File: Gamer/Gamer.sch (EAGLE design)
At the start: 44 parts, among them J1 HEADER-1X8, J2 HEADER-1X8, J3 HEADER-1X8, J4 HEADER-1X8, J5 HEADER-1X8, J6 HEADER-1X8, J7 HEADER-1X8, J8 HEADER-1X8, U1 MMA8653FCR1, U2 ATTINY48, U3 ULN2803AFWG, U4 ATTINY48, U5 ULN2803AFWG, U6 ATTINY48, U7 ULN2803AFWG, U8 ATTINY48, U9 ULN2803AFWG

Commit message: gamer - ERC passes (with many okay warnings)
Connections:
- net 3V3 renamed VCC
- removed net N$1: START.4
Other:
- note added: "3.3V"
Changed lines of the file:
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@@
 <text x="96.52" y="96.52" size="3.81" layer="91">RasPi Header</text>
 <text x="187.96" y="76.2" size="3.81" layer="91">Accelerometer</text>
+<text x="97.79" y="159.766" size="1.778" layer="91" rot="R90">3.3V</text>
 </plain>
 <instances>
@@
 </segment>
 </net>
-<net name="3V3" class="0">
+<net name="VCC" class="0">
 <segment>
 <pinref part="SUPPLY17" gate="G$1" pin="VCC"/>
@@
 </segment>
 <segment>
-<label x="96.52" y="157.48" size="1.016" layer="95" rot="R180" xref="yes"/>
 <wire x1="106.68" y1="157.48" x2="99.06" y2="157.48" width="0.1524" layer="91"/>
 <pinref part="P1" gate="A" pin="1"/>
-<wire x1="99.06" y1="157.48" x2="96.52" y2="157.48" width="0.1524" layer="91"/>
 <wire x1="99.06" y1="157.48" x2="99.06" y2="165.1" width="0.1524" layer="91"/>
-<junction x="99.06" y="157.48"/>
 <pinref part="SUPPLY29" gate="G$1" pin="VCC"/>
 </segment>
@@
 <wire x1="114.3" y1="124.46" x2="124.46" y2="124.46" width="0.1524" layer="91"/>
 <label x="124.46" y="124.46" size="1.016" layer="95" xref="yes"/>
-</segment>
-</net>
-<net name="N$1" class="0">
-<segment>
-<pinref part="START" gate="G$1" pin="4"/>
-<wire x1="60.96" y1="147.32" x2="53.34" y2="147.32" width="0.1524" layer="91"/>
 </segment>
 </net>
@@
 </segment>
 </net>
-<net name="3V3" class="0">
+<net name="VCC" class="0">
 <segment>
 <pinref part="SUPPLY1" gate="G$1" pin="VCC"/>
@@
 </segment>
 </net>
-<net name="3V3" class="0">
+<net name="VCC" class="0">
 <segment>
 <pinref part="SUPPLY6" gate="G$1" pin="VCC"/>
@@
 </segment>
 </net>
-<net name="3V3" class="0">
+<net name="VCC" class="0">
 <segment>
 <pinref part="SUPPLY13" gate="G$1" pin="VCC"/>
@@
 </segment>
 </net>
-<net name="3V3" class="0">
+<net name="VCC" class="0">
 <segment>
 <pinref part="SUPPLY23" gate="G$1" pin="VCC"/>

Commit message: gamer - first new protoype fixes... Unrouted.
- RaspberrySTEM GAMER name obscured by header
- mounting holes
- header pins flipped
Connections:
- net 10/MOSI: now also P1.20; no longer P1.19
- net 11/SCLK: now also P1.24; no longer P1.23
- net 12: now also P1.31; no longer P1.32
- net 13: now also P1.34; no longer P1.33
- net 14/TX: now also P1.7; no longer P1.8
- net 15/RX: now also P1.9; no longer P1.10
- net 16: now also P1.35; no longer P1.36
- net 17/RTS: now also P1.12; no longer P1.11
- net 18: now also P1.11; no longer P1.12
- net 19: now also P1.36; no longer P1.35
- net 2/SDA: now also P1.4; no longer P1.3
- net 20: now also P1.37; no longer P1.38
- net 21: now also P1.39; no longer P1.40
- net 22: now also P1.16; no longer P1.15
- net 23: now also P1.15; no longer P1.16
- net 24: now also P1.17; no longer P1.18
- net 25: now also P1.21; no longer P1.22
- net 26: now also P1.38; no longer P1.37
- net 27: now also P1.14; no longer P1.13
- net 3/SCL: now also P1.6; no longer P1.5
- net 3V3_2: now also P1.18; no longer P1.17
- net 4: now also P1.8; no longer P1.7
- net 5: now also P1.30; no longer P1.29
- net 5V_1: now also P1.3; no longer P1.4
- net 5V_2: now also P1.1; no longer P1.2
- net 6: now also P1.32; no longer P1.31
- net 7/CE1: now also P1.25; no longer P1.26
- net 8/CE0: now also P1.23; no longer P1.24
- net 9/MISO: now also P1.22; no longer P1.21
- net GND: now also P1.10; no longer P1.9
- net GND2: now also P1.26; no longer P1.25
- net GND3: now also P1.19; no longer P1.20
- net GND4: now also P1.13; no longer P1.14
- net GND5: now also P1.5; no longer P1.6
- net GND6: now also P1.40; no longer P1.39
- net GND7: now also P1.33; no longer P1.34
- net GND8: now also P1.29; no longer P1.30
- net ID1: now also P1.28; no longer P1.27
- net ID2: now also P1.27; no longer P1.28
- net VCC: now also P1.2; no longer P1.1

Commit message: gamer - updated BOM and silkscreen
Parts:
- renumbered A to B7, B to B8, DOWN to B6, LEFT to B4, P1 to J9, RIGHT to B5, SELECT to B2, START to B1, UP to B3

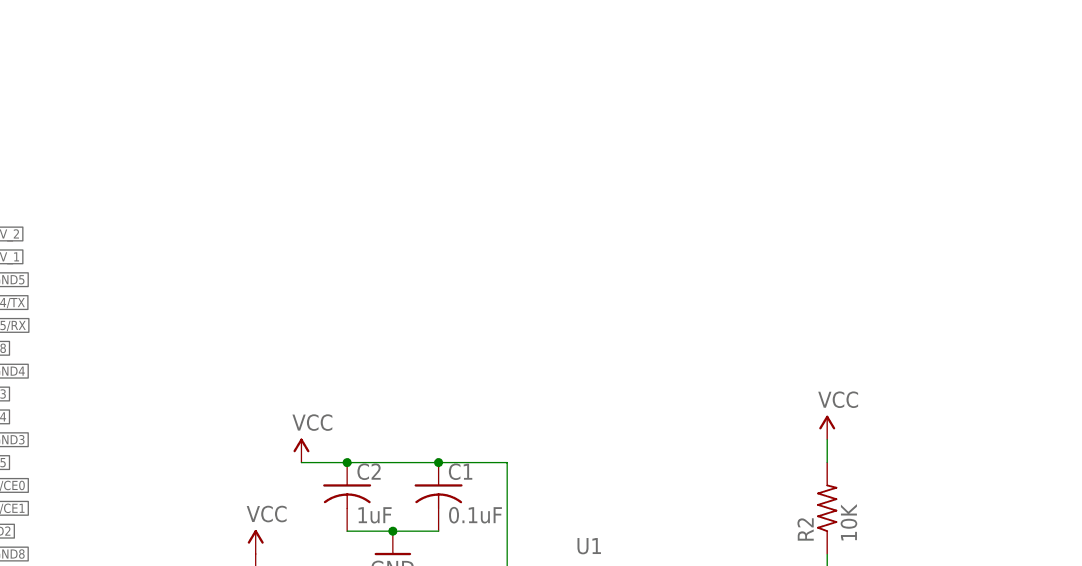
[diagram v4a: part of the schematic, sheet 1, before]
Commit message: gamer - Added EEPROM, unplaced and unrouted.
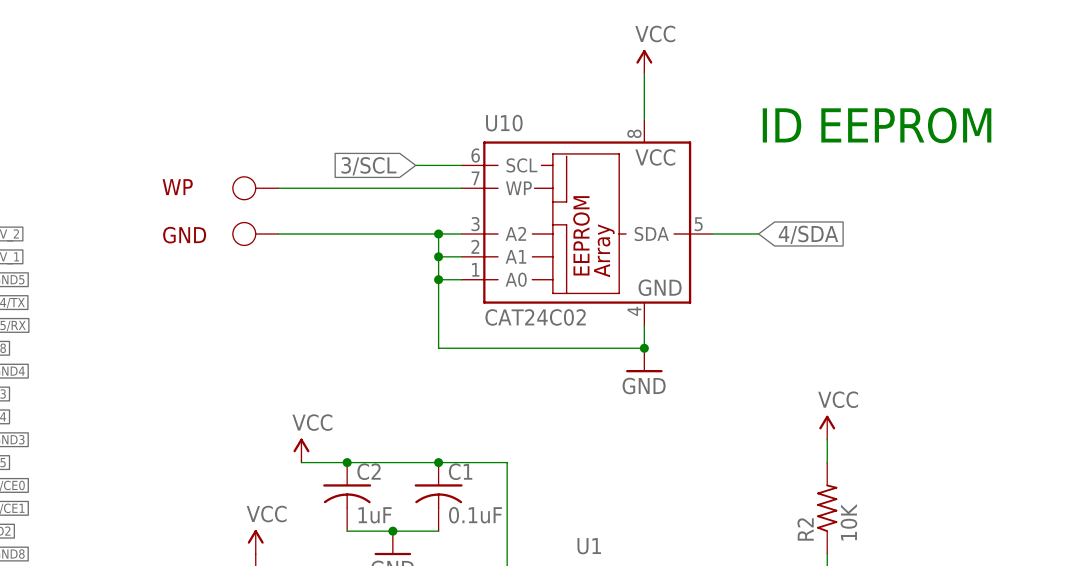
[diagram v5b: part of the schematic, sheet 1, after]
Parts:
- added GND, WP: TESTPAD, Gamer:TESTPAD
- added U10: CAT24C02, microchip:24LC64ST
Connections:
- new net 4/SDA: U10.SDA
- new net N$1: U10.WP, WP.P$1
- net 3/SCL: now also U10.SCL
- net GND: now also GND.P$1, U10.A0, U10.A1, U10.A2, U10.GND
- net VCC: now also U10.VCC
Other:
- note added: "ID EEPROM"
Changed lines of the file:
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@@
 <part name="GND30" library="SparkFun-Aesthetics" deviceset="GND" device=""/>
 <part name="R1" library="AccelBreakout" deviceset="R-US_" device="R0603" value="10K"/>
+<part name="U10" library="microchip" deviceset="24*" device="ST" technology="LC64" value="CAT24C02"/>
+<part name="GND31" library="SparkFun-Aesthetics" deviceset="GND" device=""/>
+<part name="SUPPLY30" library="SparkFun-Aesthetics" deviceset="VCC" device=""/>
+<part name="WP" library="Gamer" deviceset="TESTPAD" device=""/>
+<part name="GND" library="Gamer" deviceset="TESTPAD" device=""/>
 </parts>
 <sheets>
@@
 <text x="187.96" y="76.2" size="3.81" layer="91">Accelerometer</text>
 <text x="97.79" y="159.766" size="1.778" layer="91" rot="R90">3.3V</text>
+<text x="210.82" y="167.64" size="3.81" layer="91">ID EEPROM</text>
 </plain>
 <instances>
@@
 <instance part="GND30" gate="1" x="83.82" y="142.24"/>
 <instance part="R1" gate="G$1" x="154.94" y="116.84" rot="R90"/>
+<instance part="U10" gate="G$1" x="190.5" y="157.48"/>
+<instance part="GND31" gate="1" x="198.12" y="142.24"/>
+<instance part="SUPPLY30" gate="G$1" x="198.12" y="175.26"/>
+<instance part="WP" gate="G$1" x="157.48" y="162.56" smashed="yes" rot="R90">
+<attribute name="NAME" x="144.526" y="161.798" size="1.778" layer="94"/>
+</instance>
+<instance part="GND" gate="G$1" x="157.48" y="157.48" smashed="yes" rot="R90">
+<attribute name="NAME" x="144.526" y="156.464" size="1.778" layer="94"/>
+</instance>
 </instances>
 <busses>
@@
 <pinref part="J9" gate="A" pin="10"/>
 </segment>
+<segment>
+<pinref part="U10" gate="G$1" pin="GND"/>
+<pinref part="GND31" gate="1" pin="GND"/>
+<wire x1="198.12" y1="147.32" x2="198.12" y2="144.78" width="0.1524" layer="91"/>
+<wire x1="198.12" y1="144.78" x2="175.26" y2="144.78" width="0.1524" layer="91"/>
+<junction x="198.12" y="144.78"/>
+<wire x1="175.26" y1="144.78" x2="175.26" y2="152.4" width="0.1524" layer="91"/>
+<pinref part="U10" gate="G$1" pin="A0"/>
+<wire x1="175.26" y1="152.4" x2="177.8" y2="152.4" width="0.1524" layer="91"/>
+<wire x1="175.26" y1="152.4" x2="175.26" y2="154.94" width="0.1524" layer="91"/>
+<junction x="175.26" y="152.4"/>
+<pinref part="U10" gate="G$1" pin="A1"/>
+<wire x1="175.26" y1="154.94" x2="177.8" y2="154.94" width="0.1524" layer="91"/>
+<wire x1="175.26" y1="154.94" x2="175.26" y2="157.48" width="0.1524" layer="91"/>
+<junction x="175.26" y="154.94"/>
+<pinref part="GND" gate="G$1" pin="P$1"/>
+<wire x1="175.26" y1="157.48" x2="157.48" y2="157.48" width="0.1524" layer="91"/>
+<pinref part="U10" gate="G$1" pin="A2"/>
+<wire x1="175.26" y1="157.48" x2="177.8" y2="157.48" width="0.1524" layer="91"/>
+<junction x="175.26" y="157.48"/>
+</segment>
 </net>
 <net name="VCC" class="0">
@@
 <wire x1="106.68" y1="157.48" x2="99.06" y2="157.48" width="0.1524" layer="91"/>
 </segment>
+<segment>
+<pinref part="SUPPLY30" gate="G$1" pin="VCC"/>
+<pinref part="U10" gate="G$1" pin="VCC"/>
+<wire x1="198.12" y1="175.26" x2="198.12" y2="170.18" width="0.1524" layer="91"/>
+</segment>
 </net>
 <net name="N$34" class="0">
@@
 <wire x1="154.94" y1="111.76" x2="187.96" y2="111.76" width="0.1524" layer="91"/>
 </segment>
+<segment>
+<pinref part="U10" gate="G$1" pin="SCL"/>
+<wire x1="177.8" y1="165.1" x2="172.72" y2="165.1" width="0.1524" layer="91"/>
+<label x="172.72" y="165.1" size="1.778" layer="95" rot="R180" xref="yes"/>
+</segment>
 </net>
 <net name="4" class="0">
@@
 </segment>
 </net>
+<net name="N$1" class="0">
+<segment>
+<pinref part="U10" gate="G$1" pin="WP"/>
+<pinref part="WP" gate="G$1" pin="P$1"/>
+<wire x1="177.8" y1="162.56" x2="157.48" y2="162.56" width="0.1524" layer="91"/>
+</segment>
+</net>
+<net name="4/SDA" class="0">
+<segment>
+<pinref part="U10" gate="G$1" pin="SDA"/>
+<wire x1="205.74" y1="157.48" x2="210.82" y2="157.48" width="0.1524" layer="91"/>
+<label x="210.82" y="157.48" size="1.778" layer="95" xref="yes"/>
+</segment>
+</net>
